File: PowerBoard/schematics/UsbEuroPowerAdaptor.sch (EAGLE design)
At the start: 19 parts, among them IC1 TEC-2SIP, IC2 TBA-2SIP, J1 POWER_JACK, U4 REG_S9V11F5

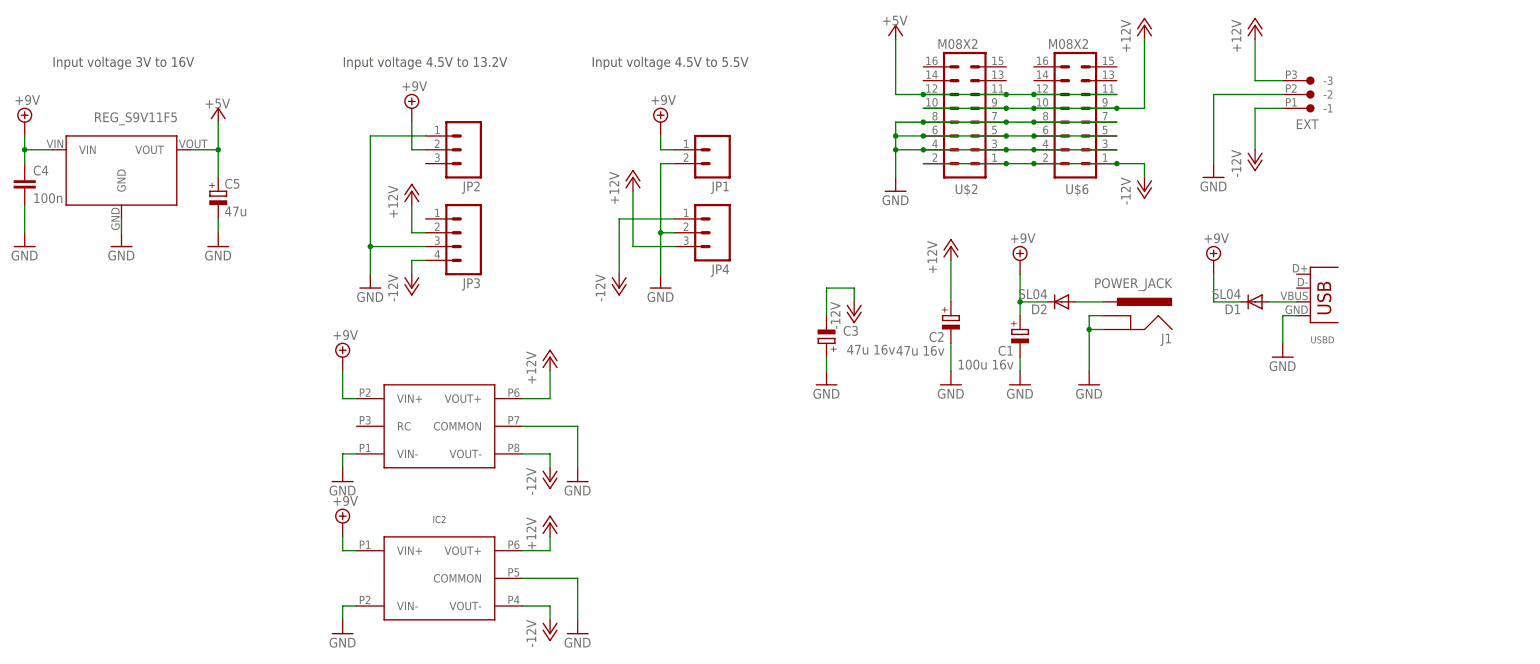
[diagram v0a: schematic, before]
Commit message: added dc converter parts
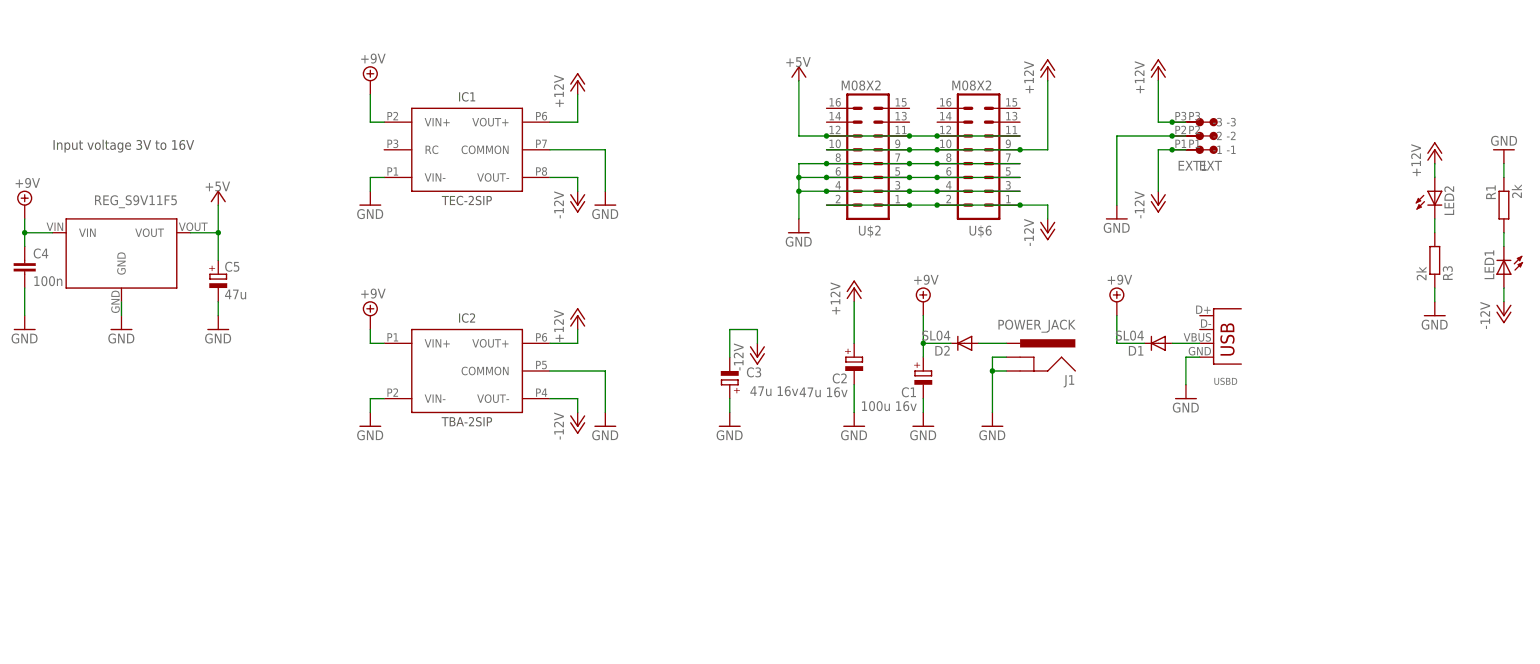
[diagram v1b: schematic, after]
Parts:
- removed JP1: (no value), SparkFun:M02PTH
- removed JP2, JP4: (no value), SparkFun:M03PTH
- removed JP3: (no value), SparkFun:M04PTH
- added EXT1: CON-JST_PH_3W, Rebel:CON-JST_PH_3W
- added LED1, LED2: (no value), Rebel:LED3MM
- added R1, R3: 2k, Rebel:R-EU_0204/7
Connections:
- new net N$1: LED2.C, R3.2
- new net N$2: LED1.C, R1.2
- net +12V: now also EXT1.-3, LED2.A; no longer JP3.2, JP4.3
- net +9V: no longer JP1.1, JP2.2
- net -12V: now also EXT1.-1, LED1.A; no longer JP3.4, JP4.1
- net GND: now also EXT1.-2, R1.1, R3.1; no longer JP1.2, JP2.1, JP3.3, JP4.2
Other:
- note removed: "Input voltage 4.5V to 13.2V"
- note removed: "Input voltage 4.5V to 5.5V"
- moved on the sheet: C1, C2, C3, C4, C5, D1, D2, EXT, IC2, J1, U$2, U$6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

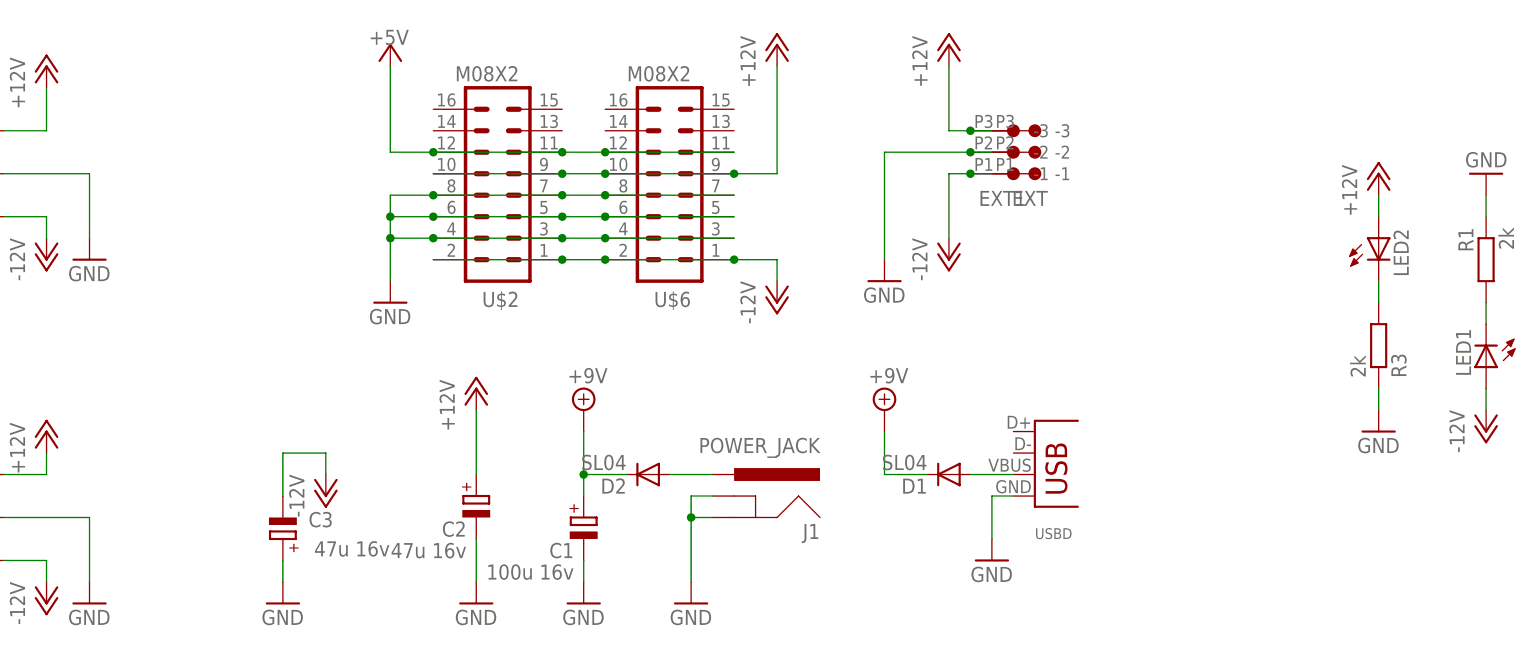
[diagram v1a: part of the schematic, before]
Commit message: USB power adaptor Rev01
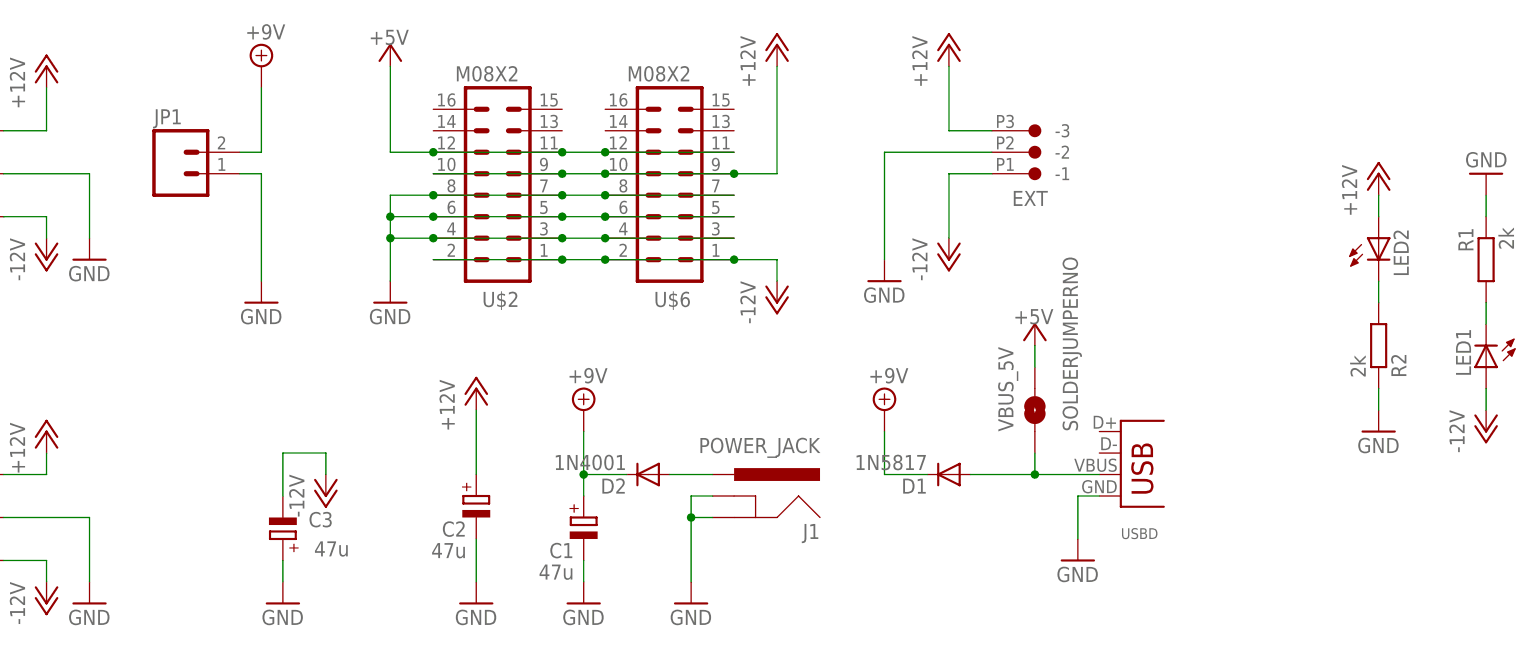
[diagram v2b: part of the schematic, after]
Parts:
- removed EXT1: CON-JST_PH_3W, Rebel:CON-JST_PH_3W
- added JP1: (no value), SparkFun:M02PTH
- added VBUS_5V: SOLDERJUMPERNO, SparkFun:SOLDERJUMPERNO
- C1: value 100u 16v -> 47u
- C2, C3: value 47u 16v -> 47u
- D1: value SL04 -> 1N5817
- D2: value SL04 -> 1N4001
- renumbered R3 to R2, U4 to IC3
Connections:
- net +12V: no longer EXT1.-3
- net +5V: now also VBUS_5V.2
- net +9V: now also JP1.2
- net -12V: no longer EXT1.-1
- net EXT_USB_D_VBUS: now also VBUS_5V.1
- net GND: now also JP1.1; no longer EXT1.-2
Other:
- moved on the sheet: USBD

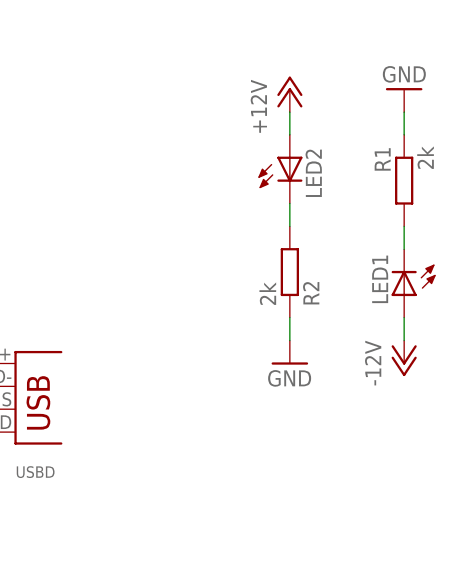
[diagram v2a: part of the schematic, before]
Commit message: Rotated leds. Changed label to Rev02
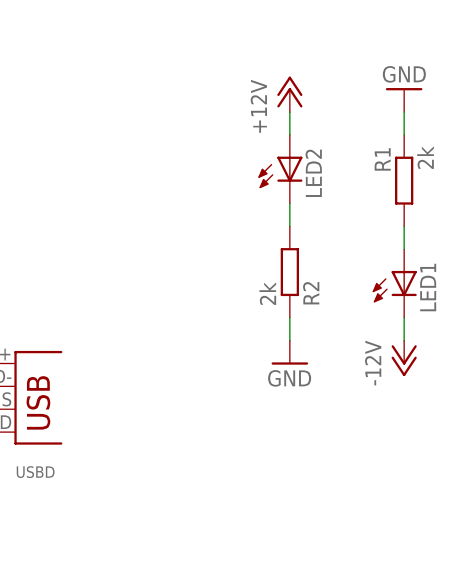
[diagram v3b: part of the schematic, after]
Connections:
- net -12V: now also LED1.C; no longer LED1.A
- net N$2: now also LED1.A; no longer LED1.C
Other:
- moved on the sheet: LED1
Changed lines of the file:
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@@
 <attribute name="VALUE" x="167.64" y="-33.02" size="1.778" layer="96"/>
 </instance>
-<instance part="LED1" gate="G$1" x="182.88" y="-22.86" smashed="yes" rot="R180">
-<attribute name="NAME" x="179.324" y="-18.288" size="1.778" layer="95" rot="R270"/>
-<attribute name="VALUE" x="177.165" y="-18.288" size="1.778" layer="96" rot="R270"/>
+<instance part="LED1" gate="G$1" x="182.88" y="-20.32" smashed="yes">
+<attribute name="NAME" x="186.436" y="-24.892" size="1.778" layer="95" rot="R90"/>
+<attribute name="VALUE" x="188.595" y="-24.892" size="1.778" layer="96" rot="R90"/>
 </instance>
 <instance part="R1" gate="G$1" x="182.88" y="-10.16" smashed="yes" rot="MR270">
@@
 </segment>
 <segment>
-<pinref part="LED1" gate="G$1" pin="A"/>
-<wire x1="182.88" y1="-27.94" x2="182.88" y2="-25.4" width="0.1524" layer="91"/>
 <pinref part="P-2" gate="1" pin="-12V"/>
+<pinref part="LED1" gate="G$1" pin="C"/>
+<wire x1="182.88" y1="-25.4" x2="182.88" y2="-27.94" width="0.1524" layer="91"/>
 </segment>
 </net>
@@
 <net name="N$2" class="0">
 <segment>
-<pinref part="LED1" gate="G$1" pin="C"/>
 <pinref part="R1" gate="G$1" pin="2"/>
-<wire x1="182.88" y1="-15.24" x2="182.88" y2="-17.78" width="0.1524" layer="91"/>
-</segment>
-</net>
+<pinref part="LED1" gate="G$1" pin="A"/>
+<wire x1="182.88" y1="-17.78" x2="182.88" y2="-15.24" width="0.1524" layer="91"/>
+</segment>
+</net>
